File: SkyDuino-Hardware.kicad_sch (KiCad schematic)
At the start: 10 parts, among them J1 PWR, U1 LV3842

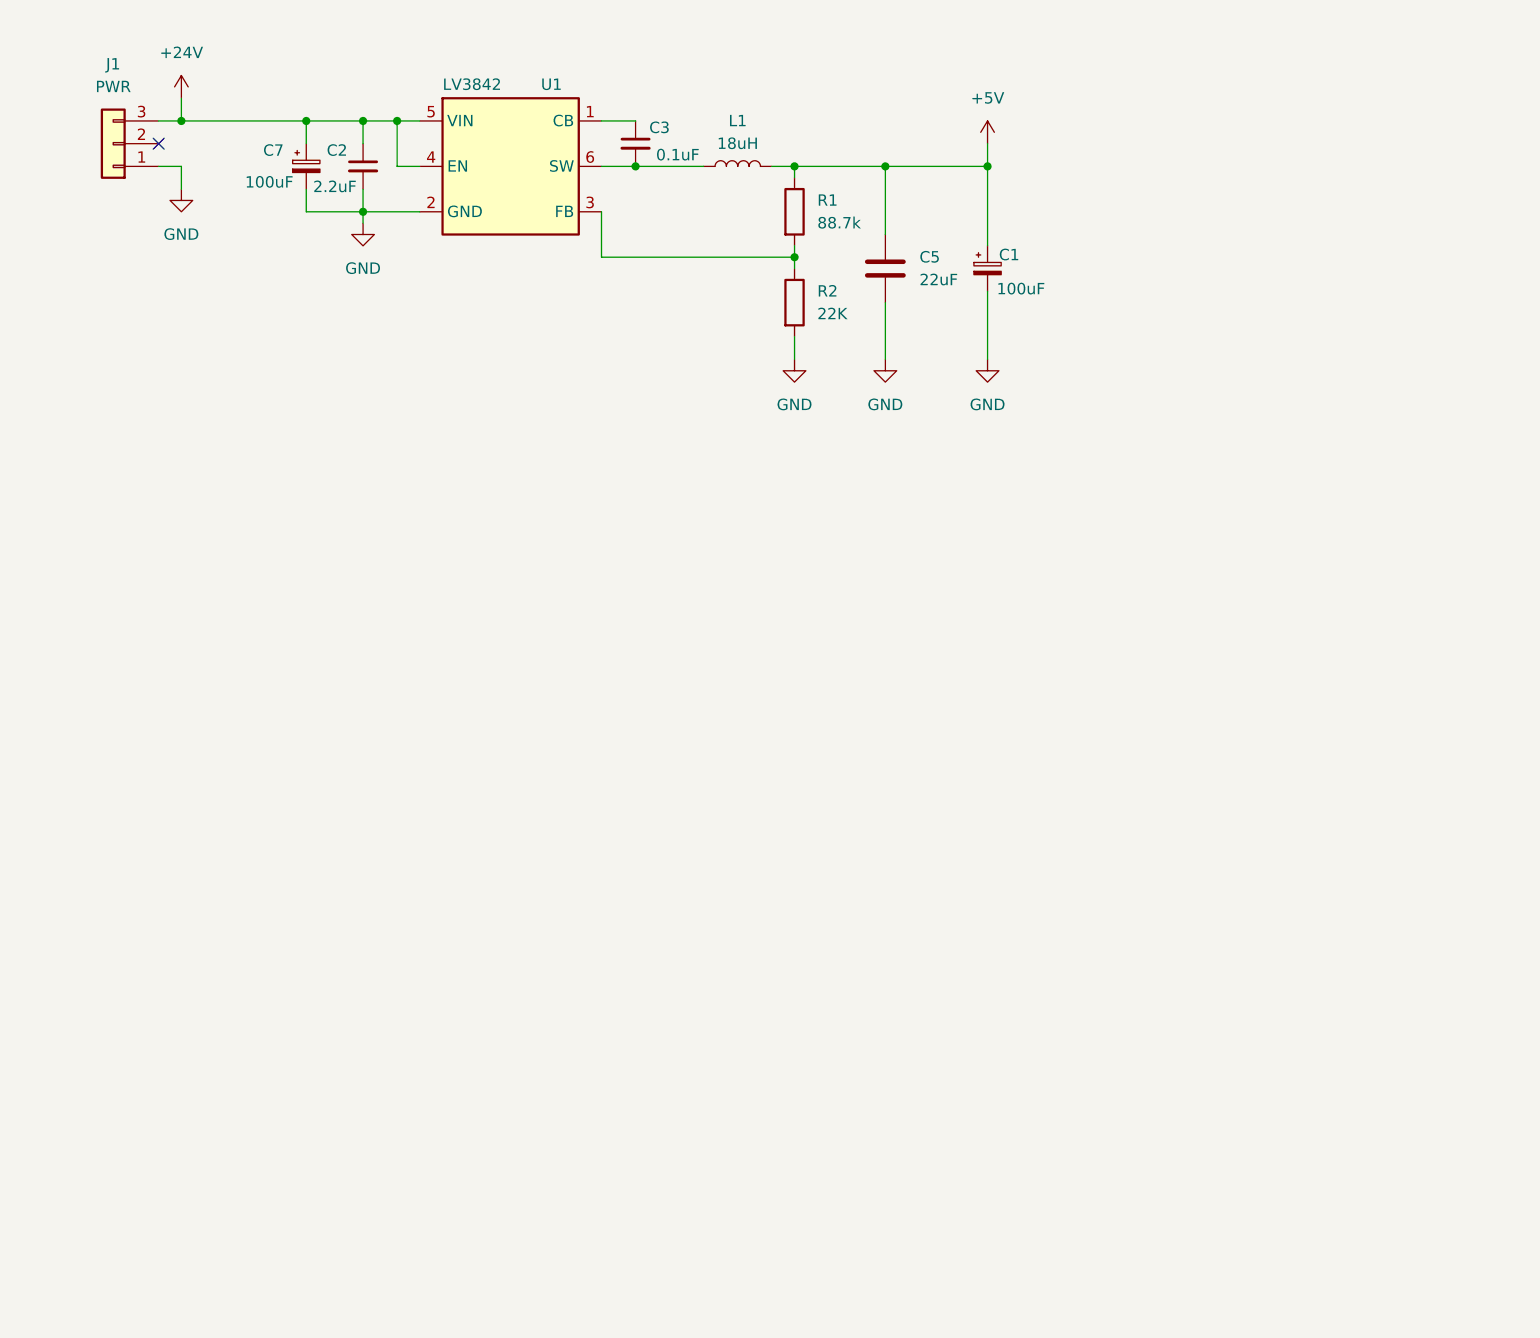
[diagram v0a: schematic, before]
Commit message: Add LDO and Motor Controls
- Add 3v3 LDO
- Add Motor controls
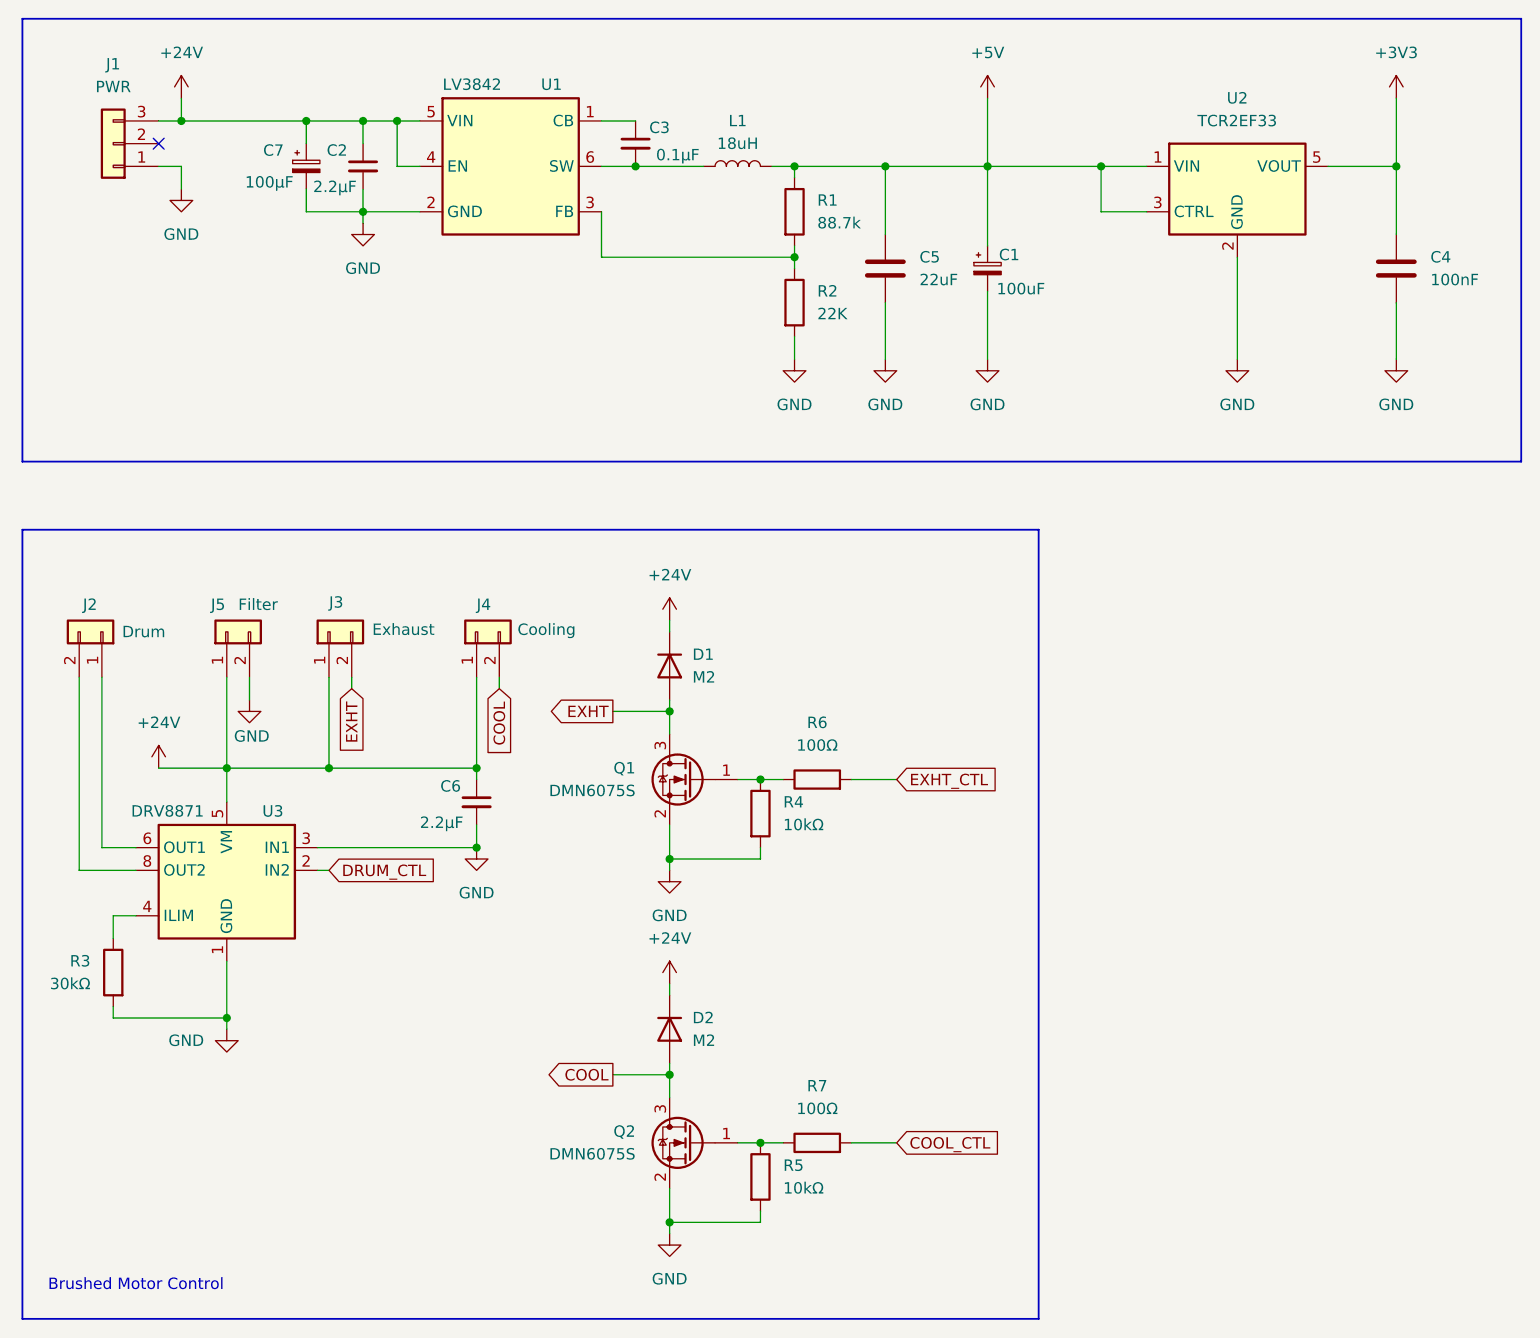
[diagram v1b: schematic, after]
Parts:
- added C4: 100nF, Capacitor_SMD:C_0805_2012Metric_Pad1.18x1.45mm_HandSolder, symbol Device:C
- added C6: 2.2µF, Capacitor_SMD:C_1210_3225Metric_Pad1.33x2.70mm_HandSolder, symbol Device:C_Small
- added D1, D2: M2, Diode_SMD:D_SMA_Handsoldering, symbol Diode:1N4002
- added J2: Drum, Connector_JST:JST_XH_B2B-XH-A_1x02_P2.50mm_Vertical, symbol Connector_Generic:Conn_01x02
- added J3: Exhaust, Connector_JST:JST_XH_B2B-XH-A_1x02_P2.50mm_Vertical, symbol Connector_Generic:Conn_01x02
- added J4: Cooling, Connector_JST:JST_XH_B2B-XH-A_1x02_P2.50mm_Vertical, symbol Connector_Generic:Conn_01x02
- added J5: Filter, Connector_JST:JST_XH_B2B-XH-A_1x02_P2.50mm_Vertical, symbol Connector_Generic:Conn_01x02
- added Q1, Q2: DMN6075S, Package_TO_SOT_SMD:SOT-23, symbol Transistor_FET:DMN6075S
- added R3: 30kΩ, Resistor_SMD:R_0805_2012Metric, symbol Device:R
- added R4, R5: 10kΩ, Resistor_SMD:R_0805_2012Metric, symbol Device:R
- added R6, R7: 100Ω, Resistor_SMD:R_0805_2012Metric, symbol Device:R
- added U2: TCR2EF33, Package_TO_SOT_SMD:SC-74A-5_1.55x2.9mm_P0.95mm, symbol Regulator_Linear:TCR2EE10
- added U3: DRV8871, Package_SO:Texas_HTSOP-8-1EP_3.9x4.9mm_P1.27mm_EP2.95x4.9mm_Mask2.4x3.1mm_ThermalVias, symbol Driver_Motor:DRV8871DDA
- C2: value 2.2uF -> 2.2µF
- C3: value 0.1uF -> 0.1µF
- C7: value 100uF -> 100µF
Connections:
- net +24V: now also C6.1, D1.1 (K), D2.1 (K), J3.1 (Pin_1), J4.1 (Pin_1), J5.1 (Pin_1), U3.5 (VM)
- net +5V: now also U2.1 (VIN), U2.3 (CTRL)
- net GND: now also C4.2, C6.2, J5.2 (Pin_2), Q1.2 (S), Q2.2 (S), R3.2, R4.2, R5.2, U2.2 (GND), U3.1 (GND), U3.3 (IN1), U3.7 (GND), U3.9 (GND)
- new net: R3.1, U3.4 (ILIM)
- new net: J2.1 (Pin_1), U3.6 (OUT1)
- new net: J2.2 (Pin_2), U3.8 (OUT2)
- new net: Q2.1 (G), R5.1, R7.1
- new net: Q1.1 (G), R4.1, R6.1
- new net +3V3: C4.1, U2.5 (VOUT)
- new net COOL: D2.2 (A), J4.2 (Pin_2), Q2.3 (D)
- new net COOL_CTL: R7.2
- new net DRUM_CTL: U3.2 (IN2)
- new net EXHT: D1.2 (A), J3.2 (Pin_2), Q1.3 (D)
- new net EXHT_CTL: R6.2
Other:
- note added: "Brushed Motor Control"

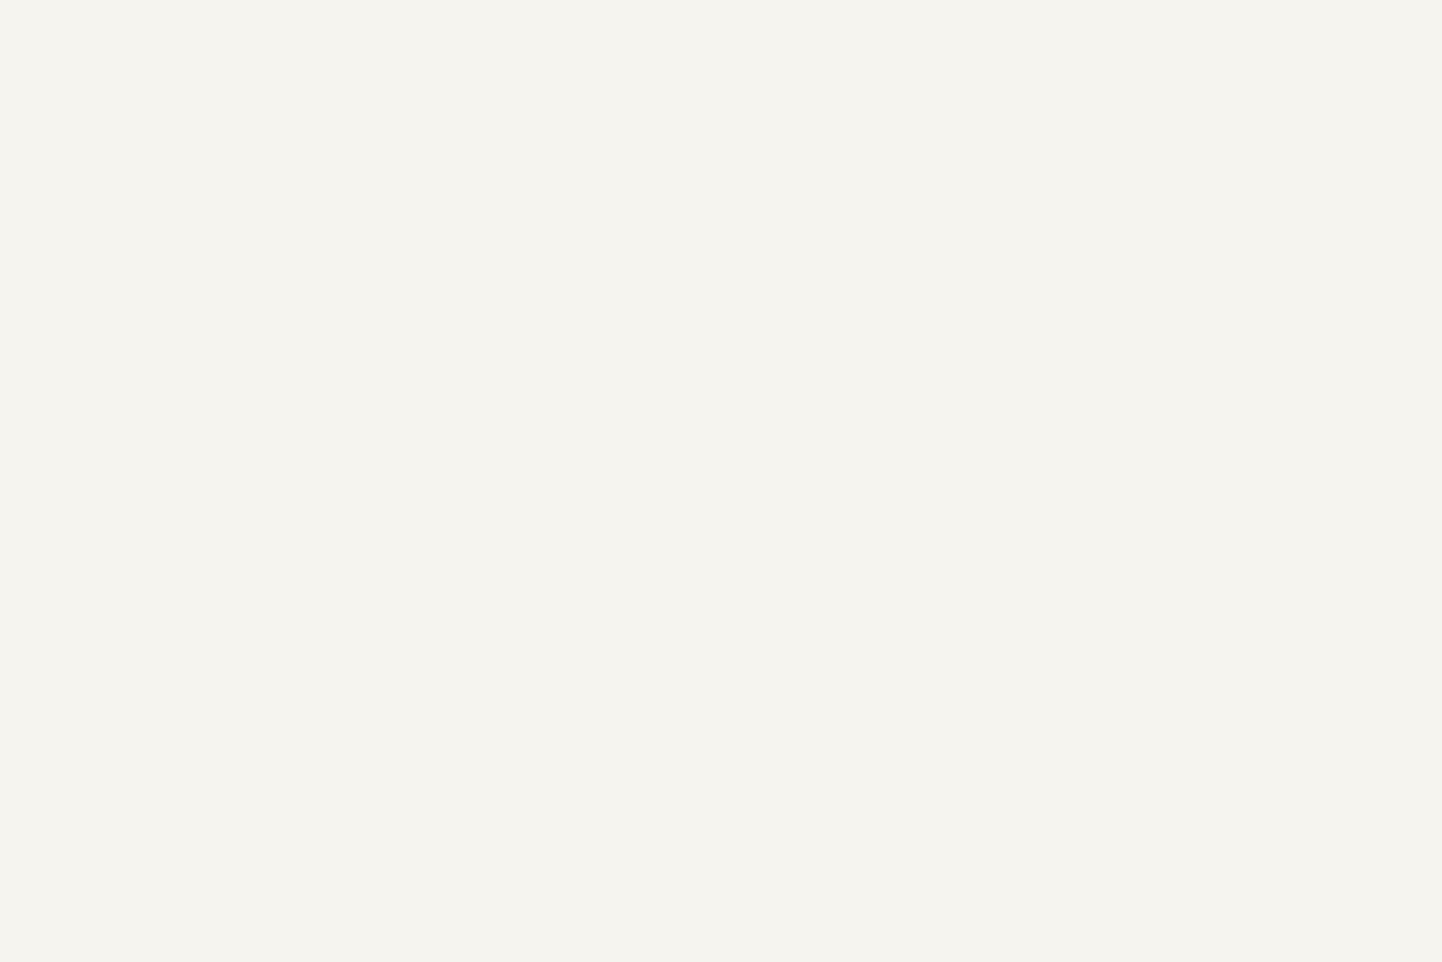
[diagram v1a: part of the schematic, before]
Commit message: Add Max33851 for BT
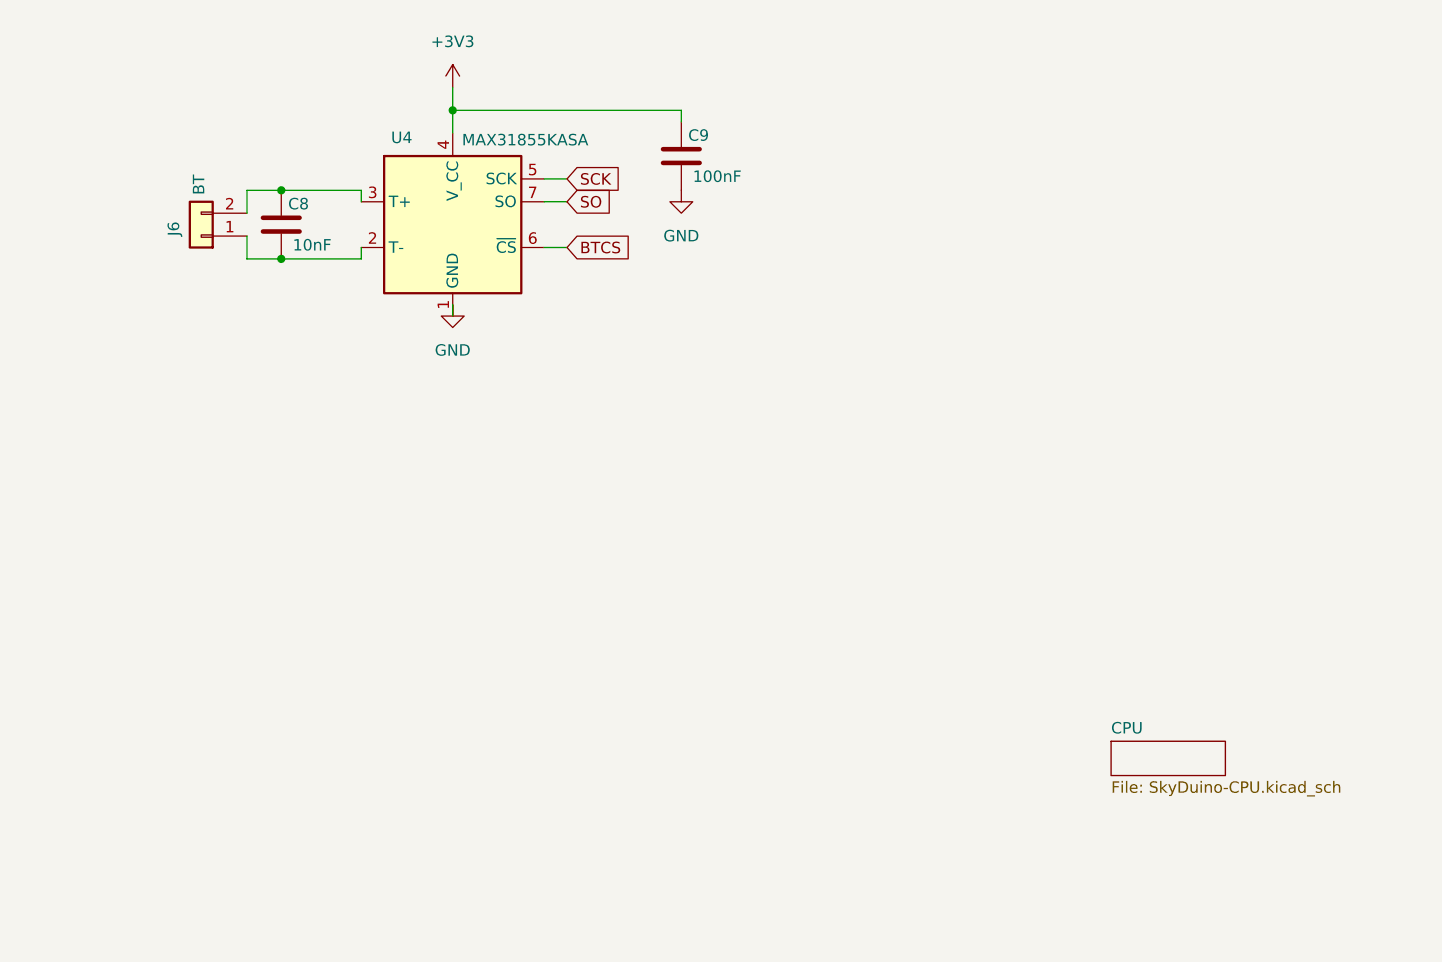
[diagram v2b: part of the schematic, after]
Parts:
- added C8: 10nF, Capacitor_SMD:C_0805_2012Metric_Pad1.18x1.45mm_HandSolder, symbol Device:C
- added C9: 100nF, Capacitor_SMD:C_0805_2012Metric_Pad1.18x1.45mm_HandSolder, symbol Device:C
- added J6: BT, Connector_JST:JST_XH_B2B-XH-A_1x02_P2.50mm_Vertical, symbol Connector_Generic:Conn_01x02
- added U4: MAX31855KASA, Package_SO:SOIC-8_3.9x4.9mm_P1.27mm, symbol Sensor_Temperature:MAX31855KASA
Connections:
- net +3V3: now also C9.1, U4.4 (V_CC)
- net GND: now also C9.2, U4.1 (GND)
- new net: C8.1, J6.2 (Pin_2), U4.3 (T+)
- new net: C8.2, J6.1 (Pin_1), U4.2 (T-)
- new net BTCS: U4.6 (~{CS})
- new net SCK: U4.5 (SCK)
- new net SO: U4.7 (SO)
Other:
- added sheet CPU (SkyDuino-CPU.kicad_sch)

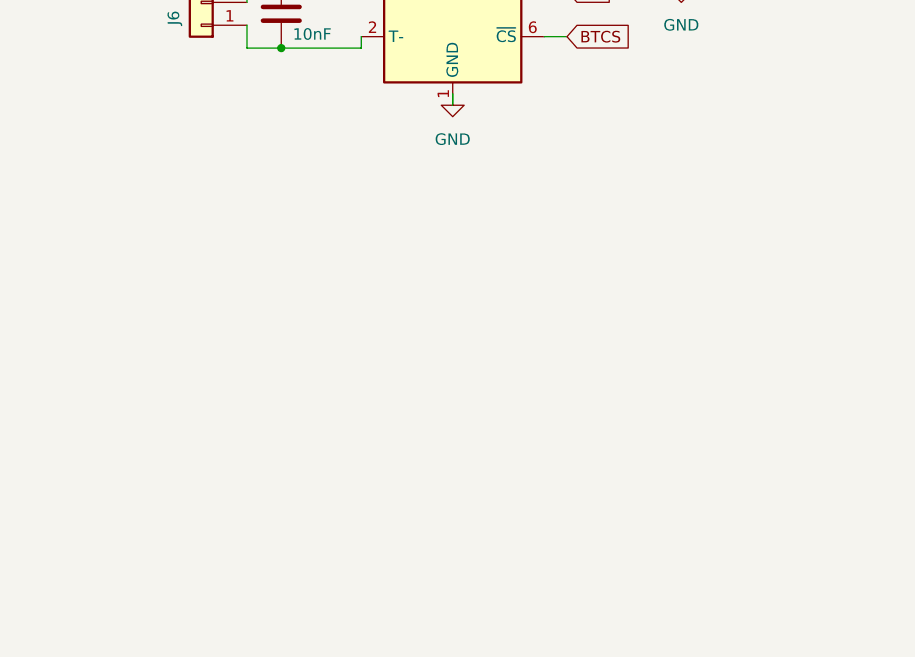
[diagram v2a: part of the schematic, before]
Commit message: Add Exhaust Temp probe
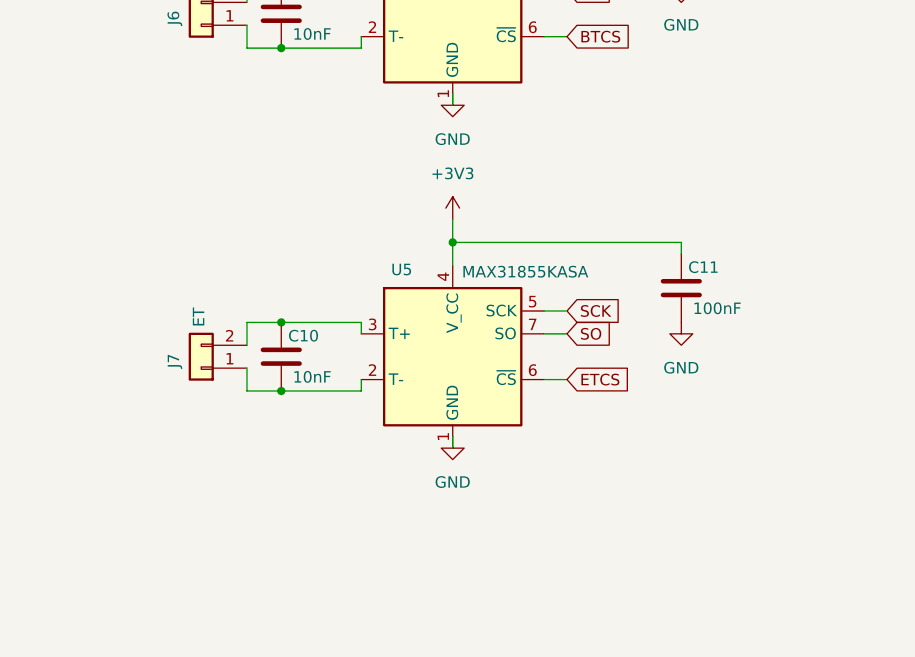
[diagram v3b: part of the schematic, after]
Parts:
- added C10: 10nF, Capacitor_SMD:C_0805_2012Metric_Pad1.18x1.45mm_HandSolder, symbol Device:C
- added C11: 100nF, Capacitor_SMD:C_0805_2012Metric_Pad1.18x1.45mm_HandSolder, symbol Device:C
- added J7: ET, Connector_SH:KF7.62_2P, symbol Connector_Generic:Conn_01x02
- added U5: MAX31855KASA, Package_SO:SOIC-8_3.9x4.9mm_P1.27mm, symbol Sensor_Temperature:MAX31855KASA
- J6: footprint Connector_JST:JST_XH_B2B-XH-A_1x02_P2.50mm_Vertical -> Connector_SH:KF7.62_2P
- L1: footprint Skyduino:L_Bourns_SRN3015BTA -> Inductor_Bourns:L_Bourns_SRN3015BTA
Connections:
- net +3V3: now also C11.1, U5.4 (V_CC)
- net GND: now also C11.2, U5.1 (GND)
- net SCK: now also U5.5 (SCK)
- net SO: now also U5.7 (SO)
- new net: C10.1, J7.2 (Pin_2), U5.3 (T+)
- new net: C10.2, J7.1 (Pin_1), U5.2 (T-)
- new net ETCS: U5.6 (~{CS})

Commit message: Rough in on MCU control connections
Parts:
- R3: Mouser pn (none) -> 603-RC0805FR-0730KL
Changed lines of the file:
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@@
 	)
 	(global_label "SO"
-		(shape input)
+		(shape output)
 		(at 252.73 72.39 0)
 		(fields_autoplaced yes)
@@
 	)
 	(global_label "SO"
-		(shape input)
+		(shape output)
 		(at 252.73 34.29 0)
 		(fields_autoplaced yes)
@@
 			)
 		)
-		(property "Datasheet" "~"
+		(property "Datasheet" "https://www.mouser.com/datasheet/2/447/YAGEO_PYu_RC_Group_51_RoHS_L_12-3313492.pdf"
 			(at 24.13 120.65 0)
 			(effects
@@
 			)
 		)
+		(property "Mouser pn" "603-RC0805FR-0730KL"
+			(at 24.13 120.65 0)
+			(effects
+				(font
+					(size 1.27 1.27)
+				)
+				(hide yes)
+			)
+		)
 		(pin "1"
 		)
@@
 	)
 	(sheet
-		(at 313.182 94.234)
+		(at 16.002 167.894)
 		(size 12.7 3.81)
-		(fields_autoplaced yes)
 		(stroke
 			(width 0.1524)
@@
 		)
 		(property "Sheetname" "CPU"
-			(at 313.182 93.5224 0)
+			(at 16.002 166.37 0)
 			(effects
 				(font
@@
 		)
 		(property "Sheetfile" "SkyDuino-CPU.kicad_sch"
-			(at 313.182 98.6286 0)
+			(at 16.002 172.2886 0)
 			(effects
 				(font

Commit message: Add two extra 24v connectors
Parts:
- added J10: AUX1, Connector_JST:JST_XH_B2B-XH-A_1x02_P2.50mm_Vertical, symbol Connector_Generic:Conn_01x02
- added J12: AUX2, Connector_JST:JST_XH_B2B-XH-A_1x02_P2.50mm_Vertical, symbol Connector_Generic:Conn_01x02
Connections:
- net +24V: now also J10.1 (Pin_1), J12.1 (Pin_1)
- net GND: now also J10.2 (Pin_2), J12.2 (Pin_2)

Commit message: Add NTC connection
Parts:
- added J13: NTC, Connector_JST:JST_XH_B2B-XH-A_1x02_P2.50mm_Vertical, symbol Connector_Generic:Conn_01x02
- added R18: 10kΩ, Resistor_SMD:R_0805_2012Metric, symbol Device:R
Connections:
- net +3V3: now also R18.1
- net GND: now also J13.2 (Pin_2)
- new net NTC: J13.1 (Pin_1), R18.2

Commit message: Re-annotate. Add NTC capacitor
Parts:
- renumbered C7 to C1, C5 to C4, C1 to C5, C4 to C6, C8 to C7, C9 to C8, C6 to C9, J12 to J10, J6 to J2, J7 to J3, J2 to J4, J3 to J6, J4 to J7, J13 to J8, J10 to J9, R6 to R4, R4 to R5, R7 to R6, R5 to R7, R18 to R8, U4 to U3, U5 to U4, U3 to U5
